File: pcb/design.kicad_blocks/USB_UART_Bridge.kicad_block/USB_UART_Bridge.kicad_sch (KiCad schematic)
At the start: 12 parts, among them J1 USB_B_Micro, U2 MCP2221A-I/ST, U3 AP2112K-3.3

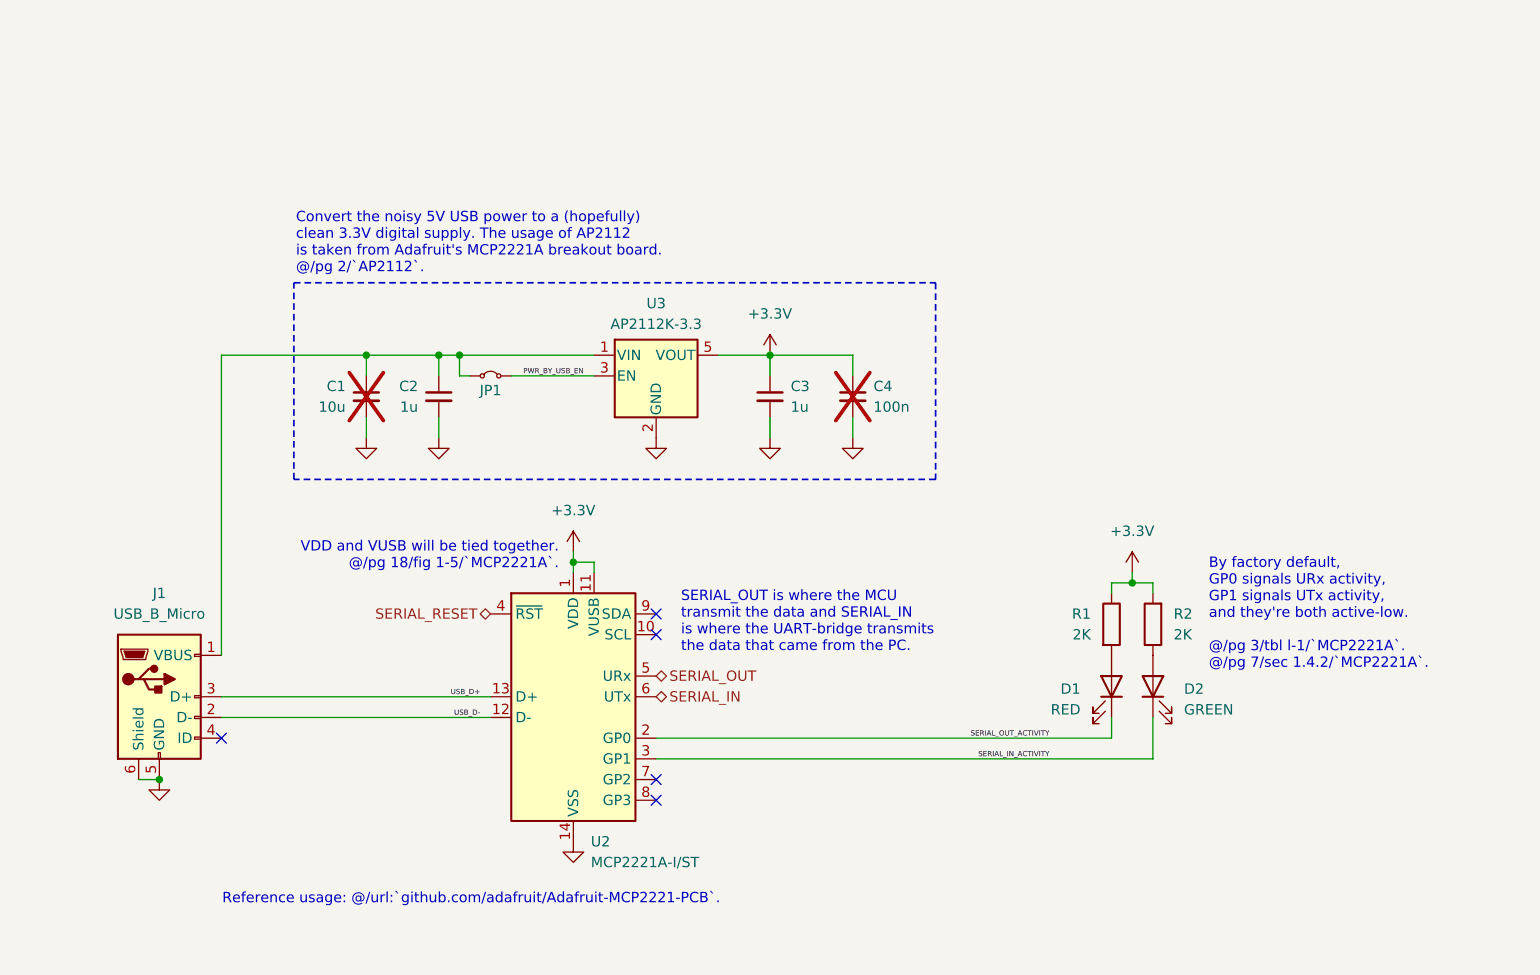
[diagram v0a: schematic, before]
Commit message: Trying out design blocks instead of hierarchal sheets.
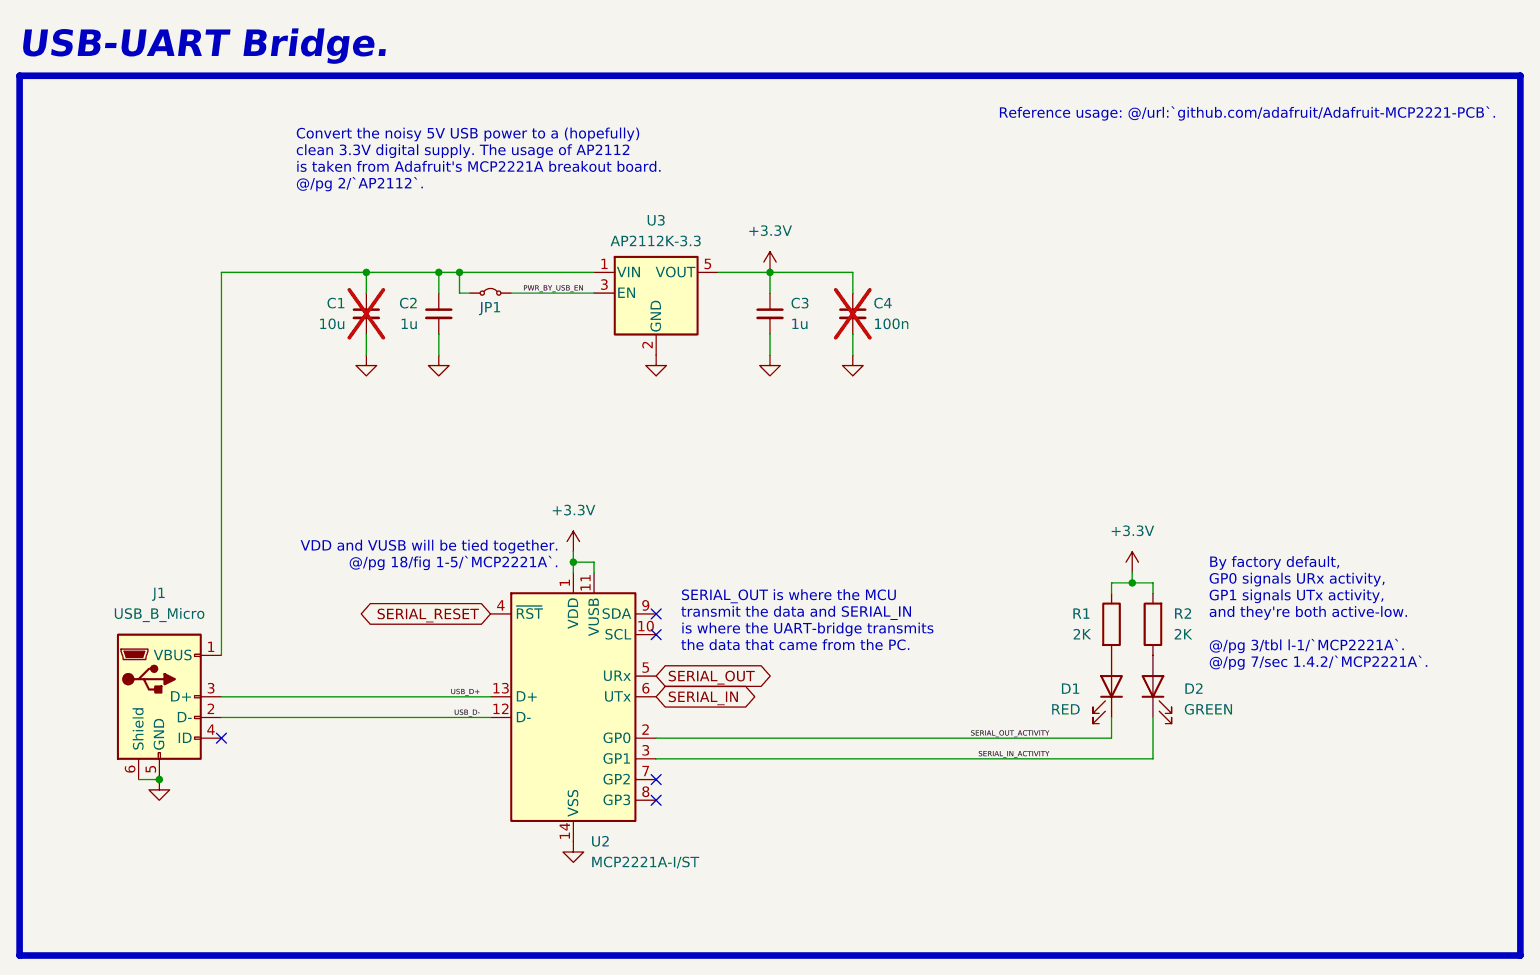
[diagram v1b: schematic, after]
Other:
- note added: "USB-UART Bridge."
- moved on the sheet: C1, C2, C3, C4, JP1, U3

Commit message: Updated the USB-UART bridge to have LEDs to indicate VBUS and +3.3V.
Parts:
- added D3, D5: GREEN, LED_SMD:LED_1206_3216Metric_Pad1.42x1.75mm_HandSolder, symbol Device:LED
- added R14, R15: 4K, Resistor_SMD:R_1206_3216Metric_Pad1.30x1.75mm_HandSolder, symbol Device:R
- renumbered C4 to C10, C1 to C7, C2 to C8, C3 to C9, JP1 to JP2, R1 to R7, R2 to R8
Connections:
- net +3.3V: now also R14.1
- net GND: now also D3.1 (K), D5.1 (K)
- net at C7.1, C8.1, J1.1 (VBUS)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: now also R15.1
- new net: D5.2 (A), R15.2
- new net: D3.2 (A), R14.2
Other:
- moved on the sheet: C10, C7, C8, C9, D1, D2, J1, JP2, R7, R8, U2, U3

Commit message: Updated USB-UART bridge to use a vertical micro-USB connector instead.
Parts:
- J1: value USB_B_Micro -> 614105150721; footprint Connector_USB:USB_Micro-B_Molex_47346-0001 -> pcb:USB_Micro-B_Wuerth_614105150721_Vertical
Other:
- note added: "USB-UART Bridge (V1 : Vertical USB)."
- note removed: "USB-UART Bridge."
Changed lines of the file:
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@@
 		)
 	)
-	(text "USB-UART Bridge."
+	(text "USB-UART Bridge (V1 : Vertical USB)."
 		(exclude_from_sim no)
 		(at 314.198 85.852 0)
@@
 			)
 		)
-		(property "Value" "USB_B_Micro"
+		(property "Value" "614105150721"
 			(at 323.85 153.67 0)
 			(effects
@@
 			)
 		)
-		(property "Footprint" "Connector_USB:USB_Micro-B_Molex_47346-0001"
+		(property "Footprint" "pcb:USB_Micro-B_Wuerth_614105150721_Vertical"
 			(at 327.66 165.1 0)
 			(effects

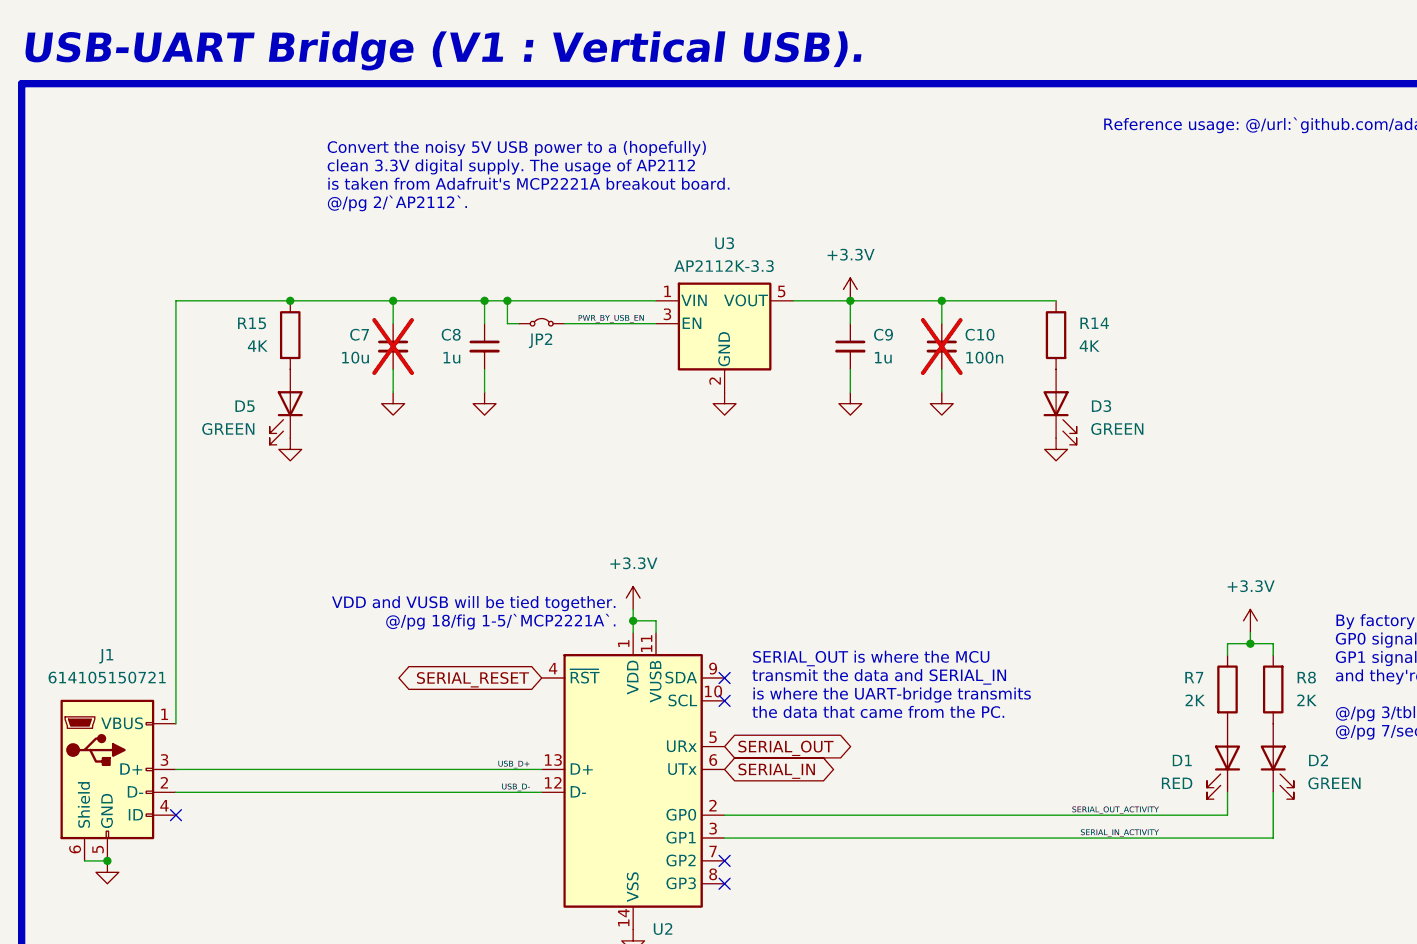
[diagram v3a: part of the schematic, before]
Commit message: USB-UART bridge connected to MCU.
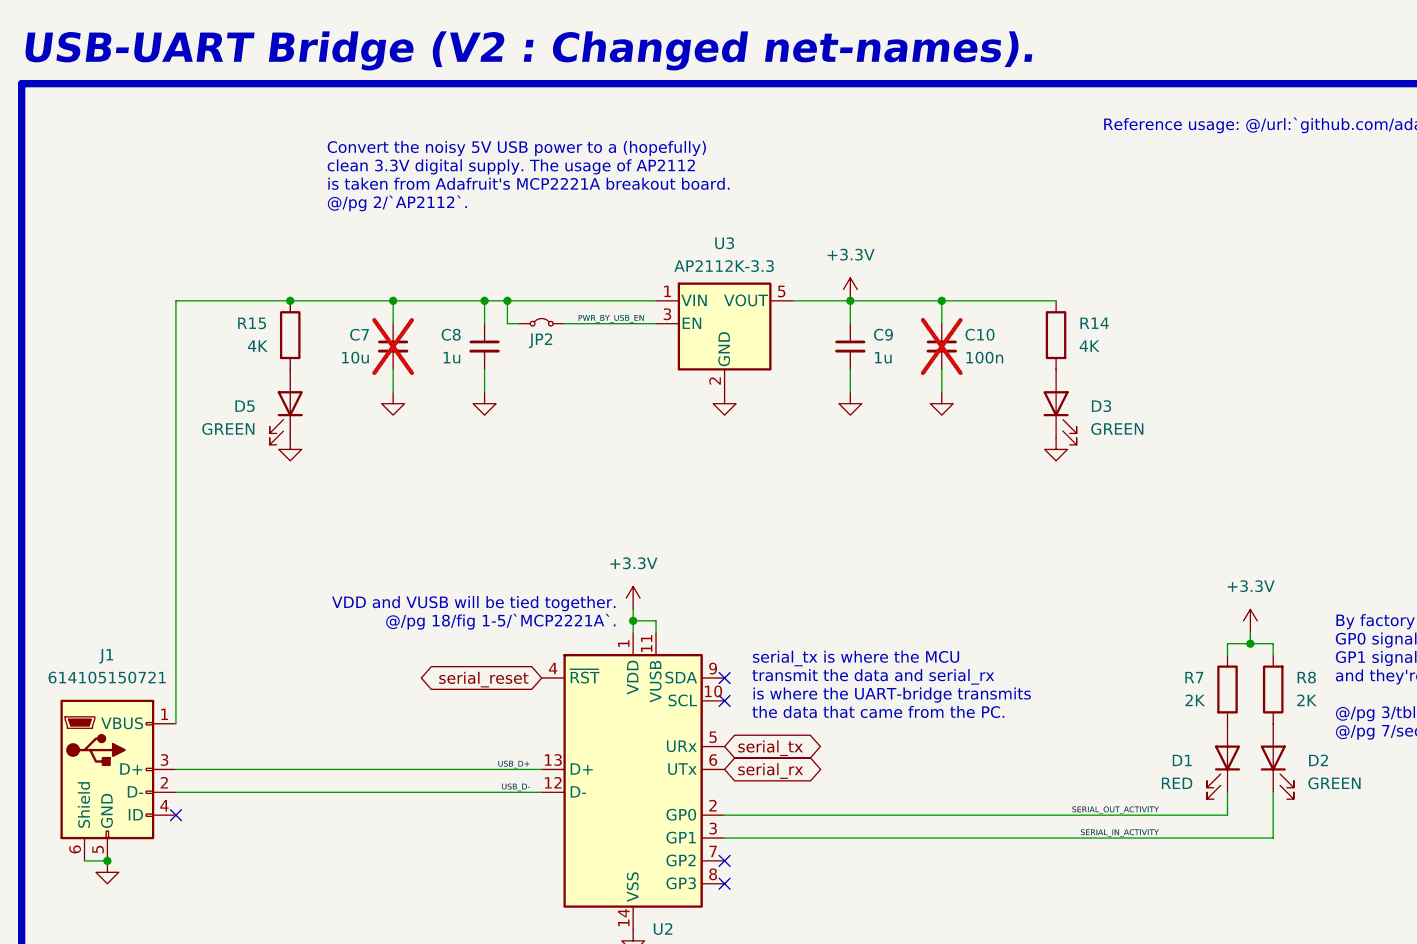
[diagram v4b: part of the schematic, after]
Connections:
- net SERIAL_IN renamed serial_rx
- net SERIAL_OUT renamed serial_tx
- net SERIAL_RESET renamed serial_reset
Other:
- note added: "USB-UART Bridge (V2 : Changed net-names)."
- note added: "serial_tx is where the MCU transmit the data and serial_rx is where the UART-bridge transmits the data that came from the PC."
- note removed: "SERIAL_OUT is where the MCU transmit the data and SERIAL_IN is where the UART-bridge transmits the data that came from the PC."
- note removed: "USB-UART Bridge (V1 : Vertical USB)."
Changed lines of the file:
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@@
 		)
 	)
-	(text "USB-UART Bridge (V1 : Vertical USB)."
+	(text "USB-UART Bridge (V2 : Changed net-names)."
 		(exclude_from_sim no)
 		(at 314.198 85.852 0)
@@
 		)
 	)
-	(text "SERIAL_OUT is where the MCU\ntransmit the data and SERIAL_IN\nis where the UART-bridge transmits\nthe data that came from the PC."
+	(text "serial_tx is where the MCU\ntransmit the data and serial_rx\nis where the UART-bridge transmits\nthe data that came from the PC."
 		(exclude_from_sim no)
 		(at 395.478 158.496 0)
@@
 		)
 	)
-	(global_label "SERIAL_RESET"
+	(global_label "serial_reset"
 		(shape bidirectional)
 		(at 372.11 153.67 180)
@@
 		)
 		(property "Intersheetrefs" "${INTERSHEET_REFS}"
-			(at 354.9508 153.67 0)
+			(at 357.0068 153.67 0)
 			(effects
 				(font
@@
 		)
 	)
-	(global_label "SERIAL_OUT"
+	(global_label "serial_tx"
 		(shape bidirectional)
 		(at 392.43 161.29 0)
@@
 		)
 		(property "Intersheetrefs" "${INTERSHEET_REFS}"
-			(at 407.4727 161.29 0)
+			(at 404.5698 161.29 0)
 			(effects
 				(font
@@
 		)
 	)
-	(global_label "SERIAL_IN"
+	(global_label "serial_rx"
 		(shape bidirectional)
 		(at 392.43 163.83 0)
@@
 		)
 		(property "Intersheetrefs" "${INTERSHEET_REFS}"
-			(at 405.7794 163.83 0)
+			(at 404.6303 163.83 0)
 			(effects
 				(font
